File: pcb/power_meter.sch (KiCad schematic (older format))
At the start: 28 parts, among them J1 USB_B, J2 AudioJack3, U1 LD1117S33TR_SOT223, U2 ATmega32U4-MU, Y1 16 MHz

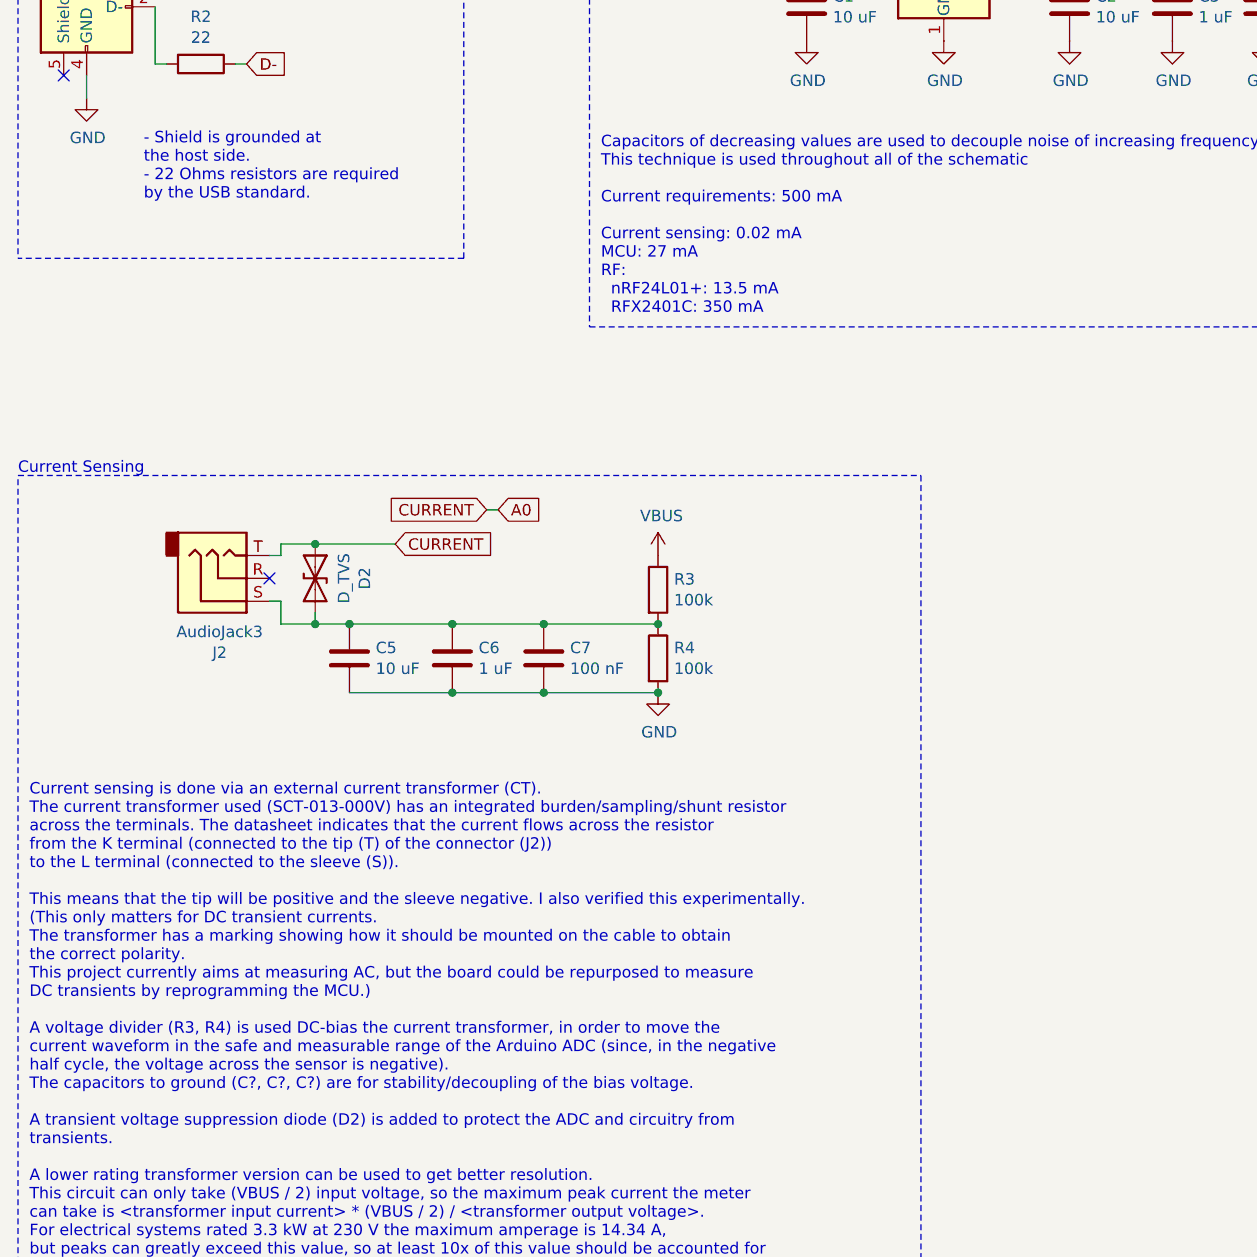
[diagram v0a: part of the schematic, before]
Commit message: small corrections, backup datasheets
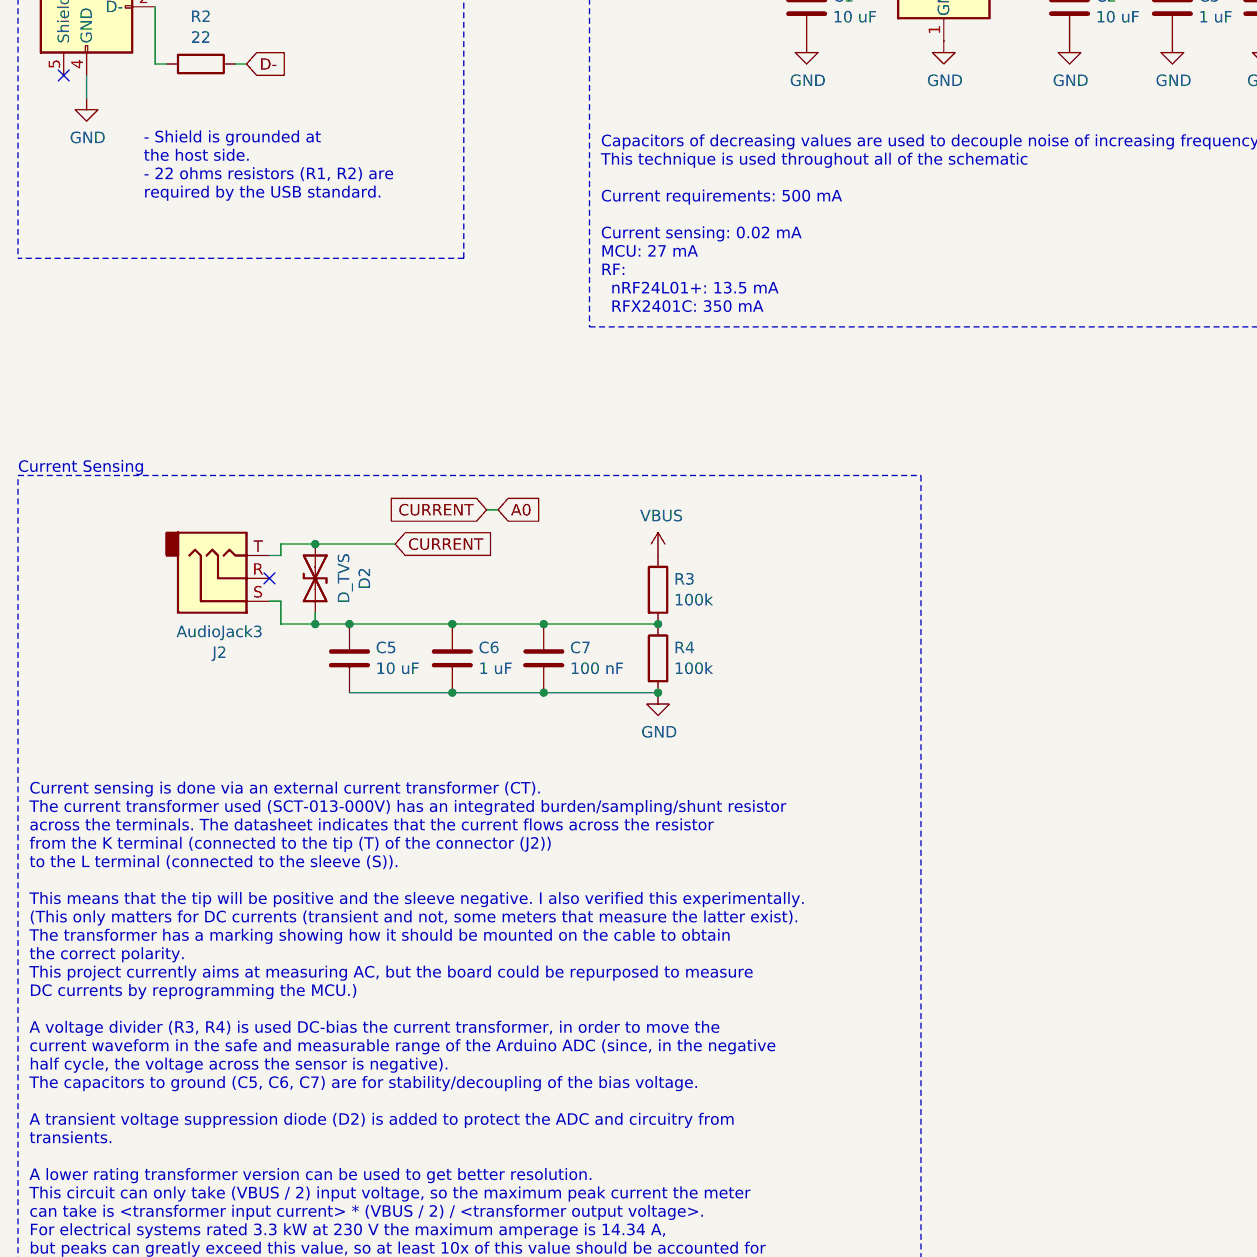
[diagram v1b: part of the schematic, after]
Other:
- note added: "- Shield is grounded at\nthe host side.\n- 22 ohms resistors (R1, R2) are\nrequired by the USB standard."
- note removed: "- Shield is grounded at\nthe host side.\n- 22 Ohms resistors are required\nby the USB standard."
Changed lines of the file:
@@
 USB Connector
 Text Notes 1150 2250 0    50   ~ 0
-- Shield is grounded at\nthe host side.\n- 22 Ohms resistors are required\nby the USB standard.
+- Shield is grounded at\nthe host side.\n- 22 ohms resistors (R1, R2) are\nrequired by the USB standard.
 Wire Wire Line
 	10650 1500 10700 1500
@@
 	1900 4050 1900 4100
 Text Notes 650  6950 0    50   ~ 0
-Current sensing is done via an external current transformer (CT).\nThe current transformer used (SCT-013-000V) has an integrated burden/sampling/shunt resistor\nacross the terminals. The datasheet indicates that the current flows across the resistor\nfrom the K terminal (connected to the tip (T) of the connector (J2))\nto the L terminal (connected to the sleeve (S)).\n\nThis means that the tip will be positive and the sleeve negative. I also verified this experimentally.\n(This only matters for DC transient currents.\nThe transformer has a marking showing how it should be mounted on the cable to obtain\nthe correct polarity.\nThis project currently aims at measuring AC, but the board could be repurposed to measure\nDC transients by reprogramming the MCU.)\n\nA voltage divider (R3, R4) is used DC-bias the current transformer, in order to move the\ncurrent waveform in the safe and measurable range of the Arduino ADC (since, in the negative\nhalf cycle, the voltage across the sensor is negative).\nThe capacitors to ground (C?, C?, C?) are for stability/decoupling of the bias voltage.\n\nA transient voltage suppression diode (D2) is added to protect the ADC and circuitry from\ntransients.\n\nA lower rating transformer version can be used to get better resolution.\nThis circuit can only take (VBUS / 2) input voltage, so the maximum peak current the meter\ncan take is <transformer input current> * (VBUS / 2) / <transformer output voltage>.\nFor electrical systems rated 3.3 kW at 230 V the maximum amperage is 14.34 A,\nbut peaks can greatly exceed this value, so at least 10x of this value should be accounted for\nin the design and transformer choice.\n
+Current sensing is done via an external current transformer (CT).\nThe current transformer used (SCT-013-000V) has an integrated burden/sampling/shunt resistor\nacross the terminals. The datasheet indicates that the current flows across the resistor\nfrom the K terminal (connected to the tip (T) of the connector (J2))\nto the L terminal (connected to the sleeve (S)).\n\nThis means that the tip will be positive and the sleeve negative. I also verified this experimentally.\n(This only matters for DC currents (transient and not, some meters that measure the latter exist).\nThe transformer has a marking showing how it should be mounted on the cable to obtain\nthe correct polarity.\nThis project currently aims at measuring AC, but the board could be repurposed to measure\nDC currents by reprogramming the MCU.)\n\nA voltage divider (R3, R4) is used DC-bias the current transformer, in order to move the\ncurrent waveform in the safe and measurable range of the Arduino ADC (since, in the negative\nhalf cycle, the voltage across the sensor is negative).\nThe capacitors to ground (C5, C6, C7) are for stability/decoupling of the bias voltage.\n\nA transient voltage suppression diode (D2) is added to protect the ADC and circuitry from\ntransients.\n\nA lower rating transformer version can be used to get better resolution.\nThis circuit can only take (VBUS / 2) input voltage, so the maximum peak current the meter\ncan take is <transformer input current> * (VBUS / 2) / <transformer output voltage>.\nFor electrical systems rated 3.3 kW at 230 V the maximum amperage is 14.34 A,\nbut peaks can greatly exceed this value, so at least 10x of this value should be accounted for\nin the design and transformer choice.\n
 NoConn ~ 1700 3900
 $Comp
